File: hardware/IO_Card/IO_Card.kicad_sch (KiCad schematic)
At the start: 18 parts, among them J1 6502 Edge, J2 6502 Pinheader, J3 Port A, J4 Port B, J7 Port A, J8 Port B, J9 VIA IO Select, U1 W65C22NxP, U2 W65C22NxP

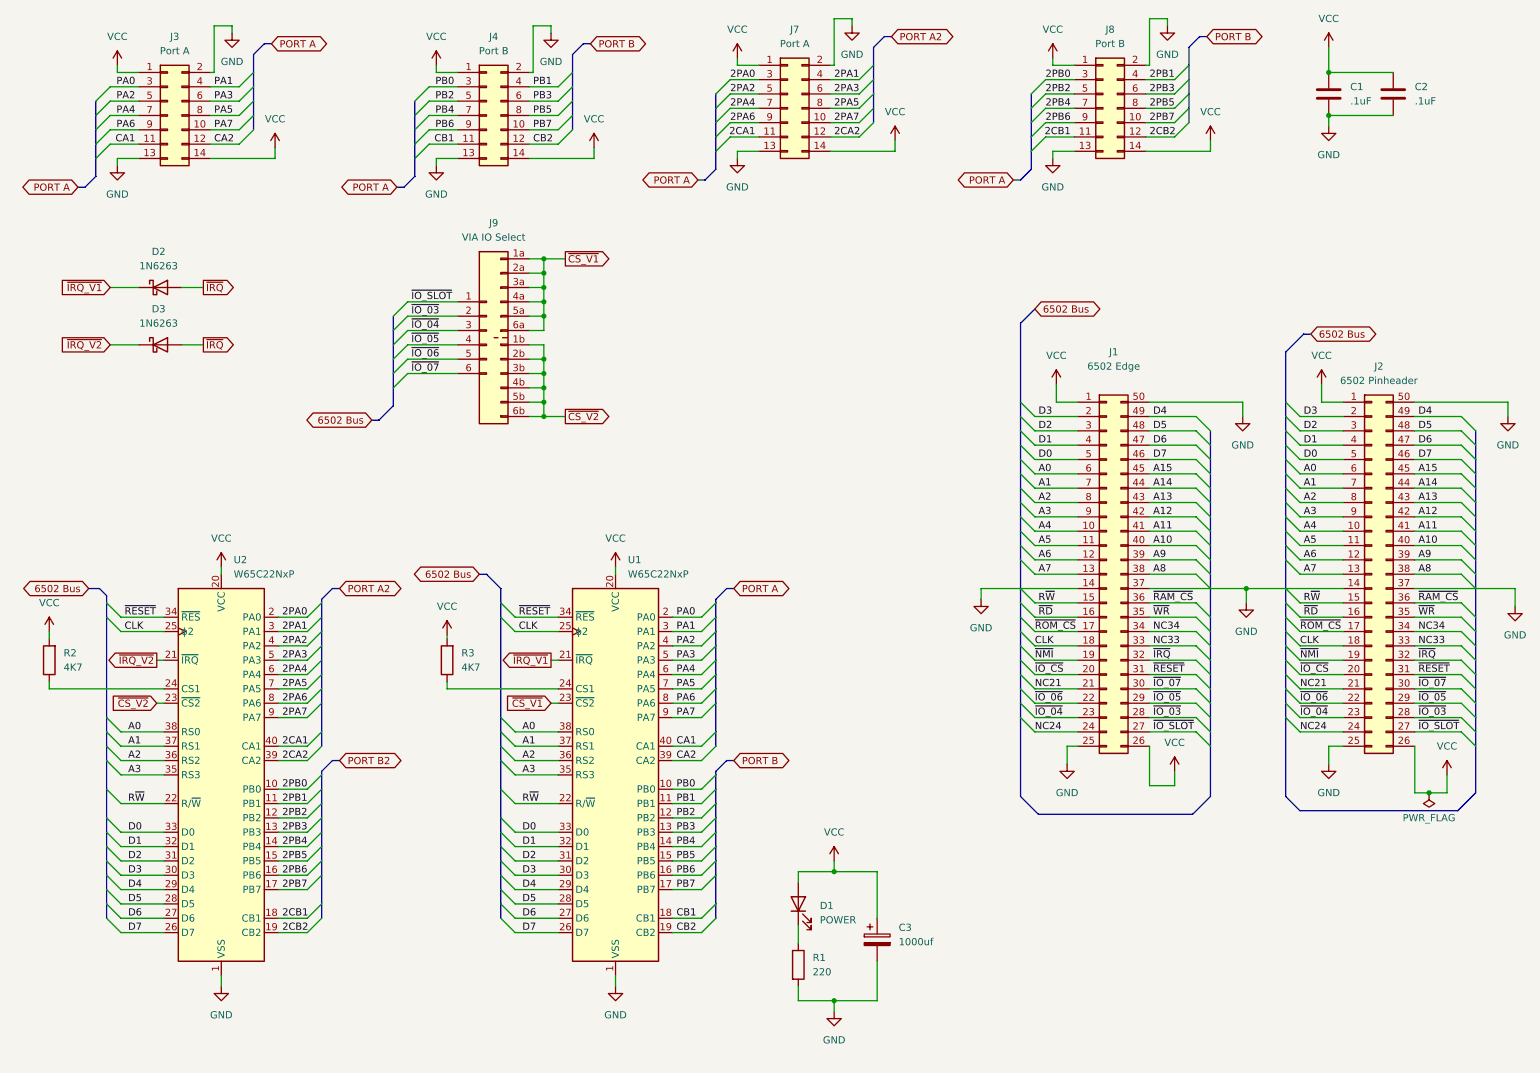
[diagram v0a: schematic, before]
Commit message: Updated to Kicad 10 - IO Card added a PS2 port
multiple model and footprint updates
PS/2 via PIC added to the IO card
Project updated to Kicad 10
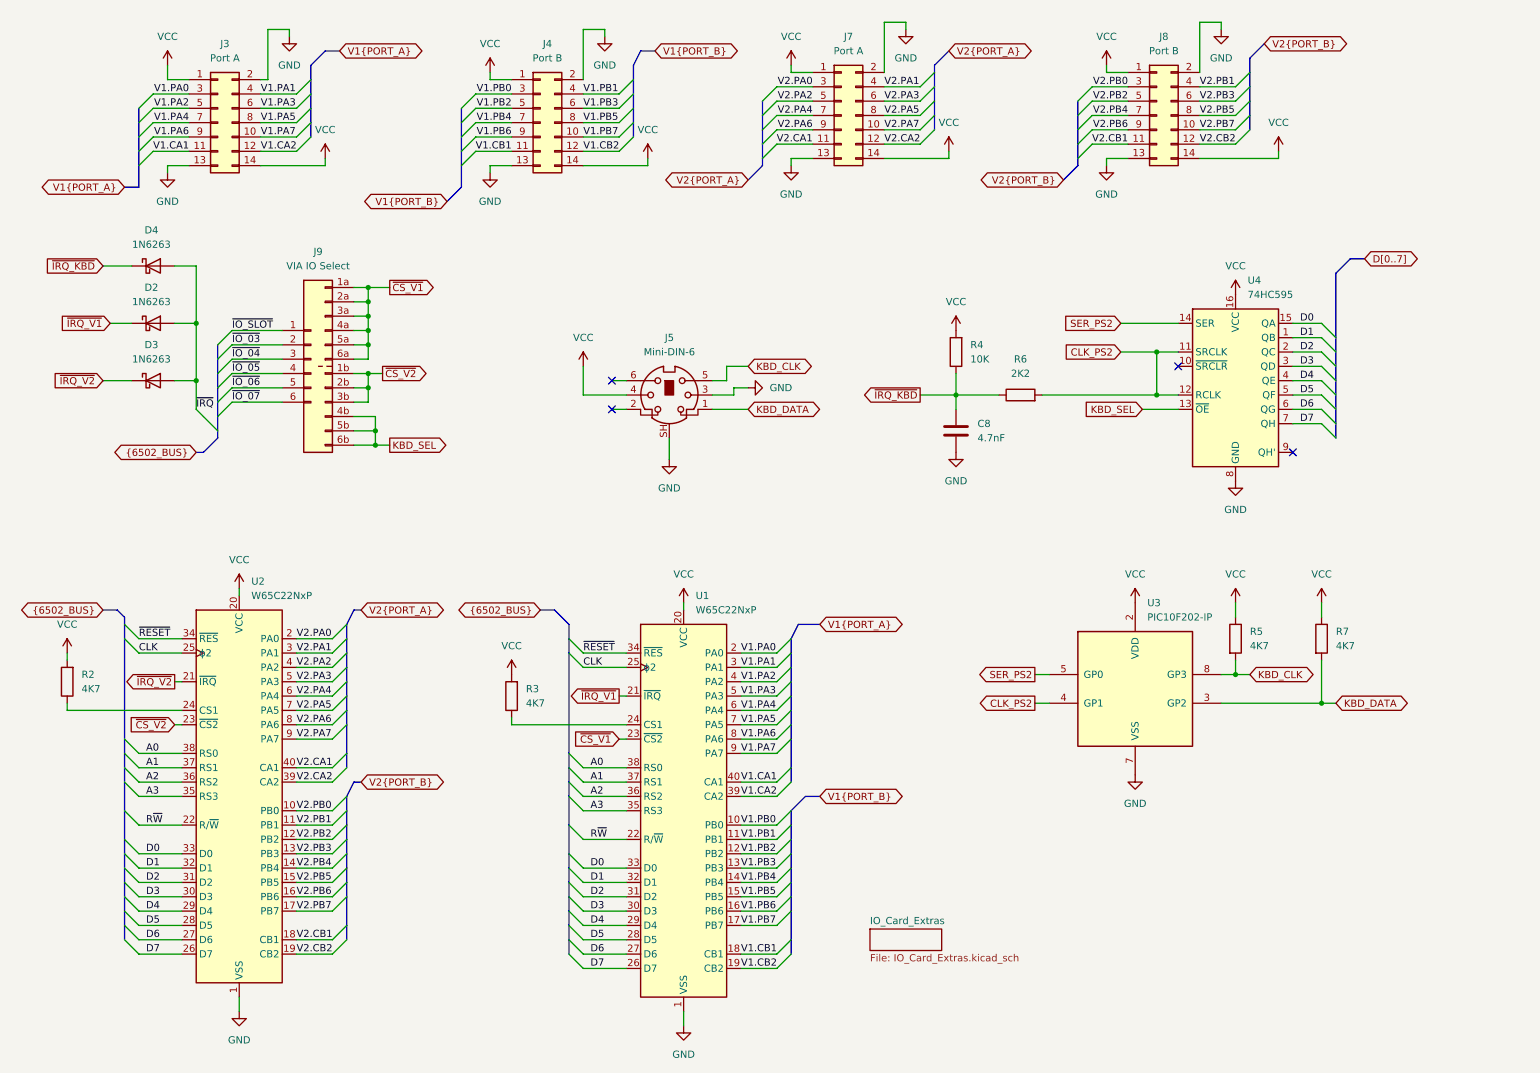
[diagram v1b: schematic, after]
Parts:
- removed C1, C2: .1uF, Capacitor_SMD:C_1206_3216Metric_Pad1.33x1.80mm_HandSolder, symbol Device:C
- removed C3: 1000uf, Capacitor_THT:CP_Radial_D5.0mm_P2.50mm, symbol Device:C_Polarized
- removed D1: POWER, LED_THT:LED_D3.0mm, symbol Device:LED
- removed J1: 6502 Edge, Connector_PCBEdge:BUS_EdgePCB_Apple_2, symbol Connector_Generic:Conn_02x25_Counter_Clockwise
- removed J2: 6502 Pinheader, Connector_PinHeader_2.54mm:PinHeader_2x25_P2.54mm_Vertical_Counter_Clockwise, symbol Connector_Generic:Conn_02x25_Counter_Clockwise
- removed R1: 220, Resistor_THT:R_Axial_DIN0207_L6.3mm_D2.5mm_P10.16mm_Horizontal, symbol Device:R
- added C8: 4.7nF, Capacitor_THT:C_Disc_D5.0mm_W2.5mm_P5.00mm, symbol Device:C
- added D4: 1N6263, Diode_THT:D_DO-35_SOD27_P7.62mm_Horizontal, symbol Diode:1N6263
- added J5: Mini-DIN-6, 6502_Components:J_Mini-DIN-6-Shield, symbol 6502_Components:PS2-Mini-DIN-6-Shield
- added R4: 10K, Resistor_THT:R_Axial_DIN0207_L6.3mm_D2.5mm_P7.62mm_Horizontal, symbol Device:R
- added R5, R7: 4K7, Resistor_THT:R_Axial_DIN0207_L6.3mm_D2.5mm_P7.62mm_Horizontal, symbol Device:R
- added R6: 2K2, Resistor_THT:R_Axial_DIN0207_L6.3mm_D2.5mm_P7.62mm_Horizontal, symbol Device:R
- added U3: PIC10F202-IP, Package_DIP:DIP-8_W7.62mm, symbol MCU_Microchip_PIC10:PIC10F202-IP
- added U4: 74HC595, Package_DIP:DIP-16_W7.62mm, symbol 74xx:74HC595
- J9: footprint Connector_PinHeader_2.54mm:PinHeader_3x06_P2.54mm_Vertical -> 6502_Components:PinHeader_3x06_P2.54mm_A_B_Vertical; symbol Connector_Generic:Conn_03x06_AB_Select_Letter_Last -> 6502_Components:Conn_03x06_AB_Select_Letter_Last
- U1, U2: symbol PCM_65xx-library:W65C22NxP -> 65xx-library:W65C22NxP
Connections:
- net D0: now also U4.15 (QA)
- net D1: now also U4.1 (QB)
- net D2: now also U4.2 (QC)
- net D3: now also U4.3 (QD)
- net D4: now also U4.4 (QE)
- net D5: now also U4.5 (QF)
- net D6: now also U4.6 (QG)
- net D7: now also U4.7 (QH)
- net GND: now also C8.2, J5.3, J5.SH, U3.7 (VSS), U4.8 (GND)
- net VCC: now also J5.4, R4.2, R5.1, R7.1, U3.2 (VDD), U4.16 (VCC)
- net ~{CS_V2}: no longer J9.4b (Pin_4b), J9.5b (Pin_5b), J9.6b (Pin_6b)
- net ~{IRQ}: now also D4.2 (A)
- net 2CA1 renamed V2.CA1
- net 2CA2 renamed V2.CA2
- net 2CB1 renamed V2.CB1
- net 2CB2 renamed V2.CB2
- net 2PA0 renamed V2.PA0
- net 2PA1 renamed V2.PA1
- net 2PA2 renamed V2.PA2
- net 2PA3 renamed V2.PA3
- net 2PA4 renamed V2.PA4
- net 2PA5 renamed V2.PA5
- net 2PA6 renamed V2.PA6
- net 2PA7 renamed V2.PA7
- net 2PB0 renamed V2.PB0
- net 2PB1 renamed V2.PB1
- net 2PB2 renamed V2.PB2
- net 2PB3 renamed V2.PB3
- net 2PB4 renamed V2.PB4
- net 2PB5 renamed V2.PB5
- net 2PB6 renamed V2.PB6
- net 2PB7 renamed V2.PB7
- net CA1 renamed V1.CA1
- net CA2 renamed V1.CA2
- net CB1 renamed V1.CB1
- net CB2 renamed V1.CB2
- net PA0 renamed V1.PA0
- net PA1 renamed V1.PA1
- net PA2 renamed V1.PA2
- net PA3 renamed V1.PA3
- net PA4 renamed V1.PA4
- net PA5 renamed V1.PA5
- net PA6 renamed V1.PA6
- net PA7 renamed V1.PA7
- net PB0 renamed V1.PB0
- net PB1 renamed V1.PB1
- net PB2 renamed V1.PB2
- net PB3 renamed V1.PB3
- net PB4 renamed V1.PB4
- net PB5 renamed V1.PB5
- net PB6 renamed V1.PB6
- net PB7 renamed V1.PB7
- new net CLK_PS2: R6.2, U3.4 (GP1), U4.11 (SRCLK), U4.12 (RCLK)
- new net KBD_CLK: J5.5, R5.2, U3.8 (GP3)
- new net KBD_DATA: J5.1, R7.2, U3.3 (GP2)
- new net KBD_SEL: J9.4b (Pin_4b), J9.5b (Pin_5b), J9.6b (Pin_6b), U4.13 (~{OE})
- new net SER_PS2: U3.5 (GP0), U4.14 (SER)
- new net ~{IRQ_KBD}: C8.1, D4.1 (K), R4.1, R6.1
- no-connect marks 0 -> 4
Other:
- added sheet IO_Card_Extras (IO_Card_Extras.kicad_sch)
- moved on the sheet: D2, D3, J3, J4, J7, J8, J9, R2, R3, U1, U2
